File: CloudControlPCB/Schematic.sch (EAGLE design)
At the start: 4 parts, among them J1 AUDIO_JACK_TRRSSMD_RA, U1 LPC4088FBD208, U2 SGTL5000XNLA3R2

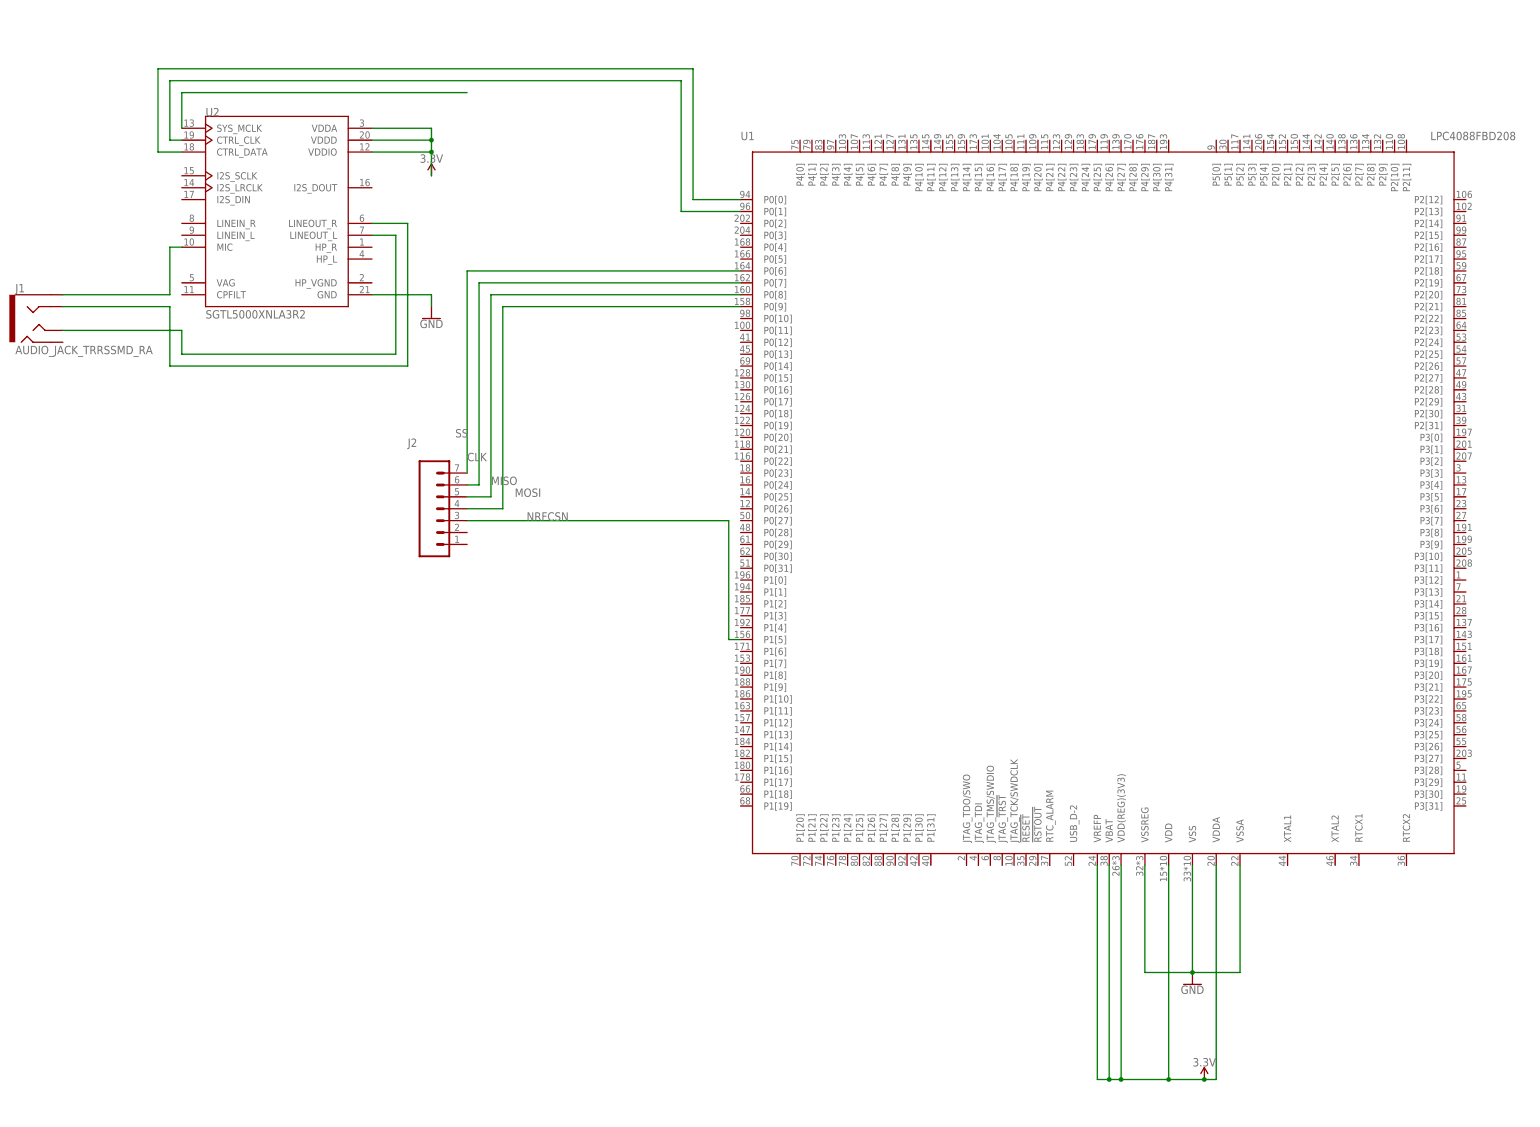
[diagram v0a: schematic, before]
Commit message: Added connections to DAC for I2S
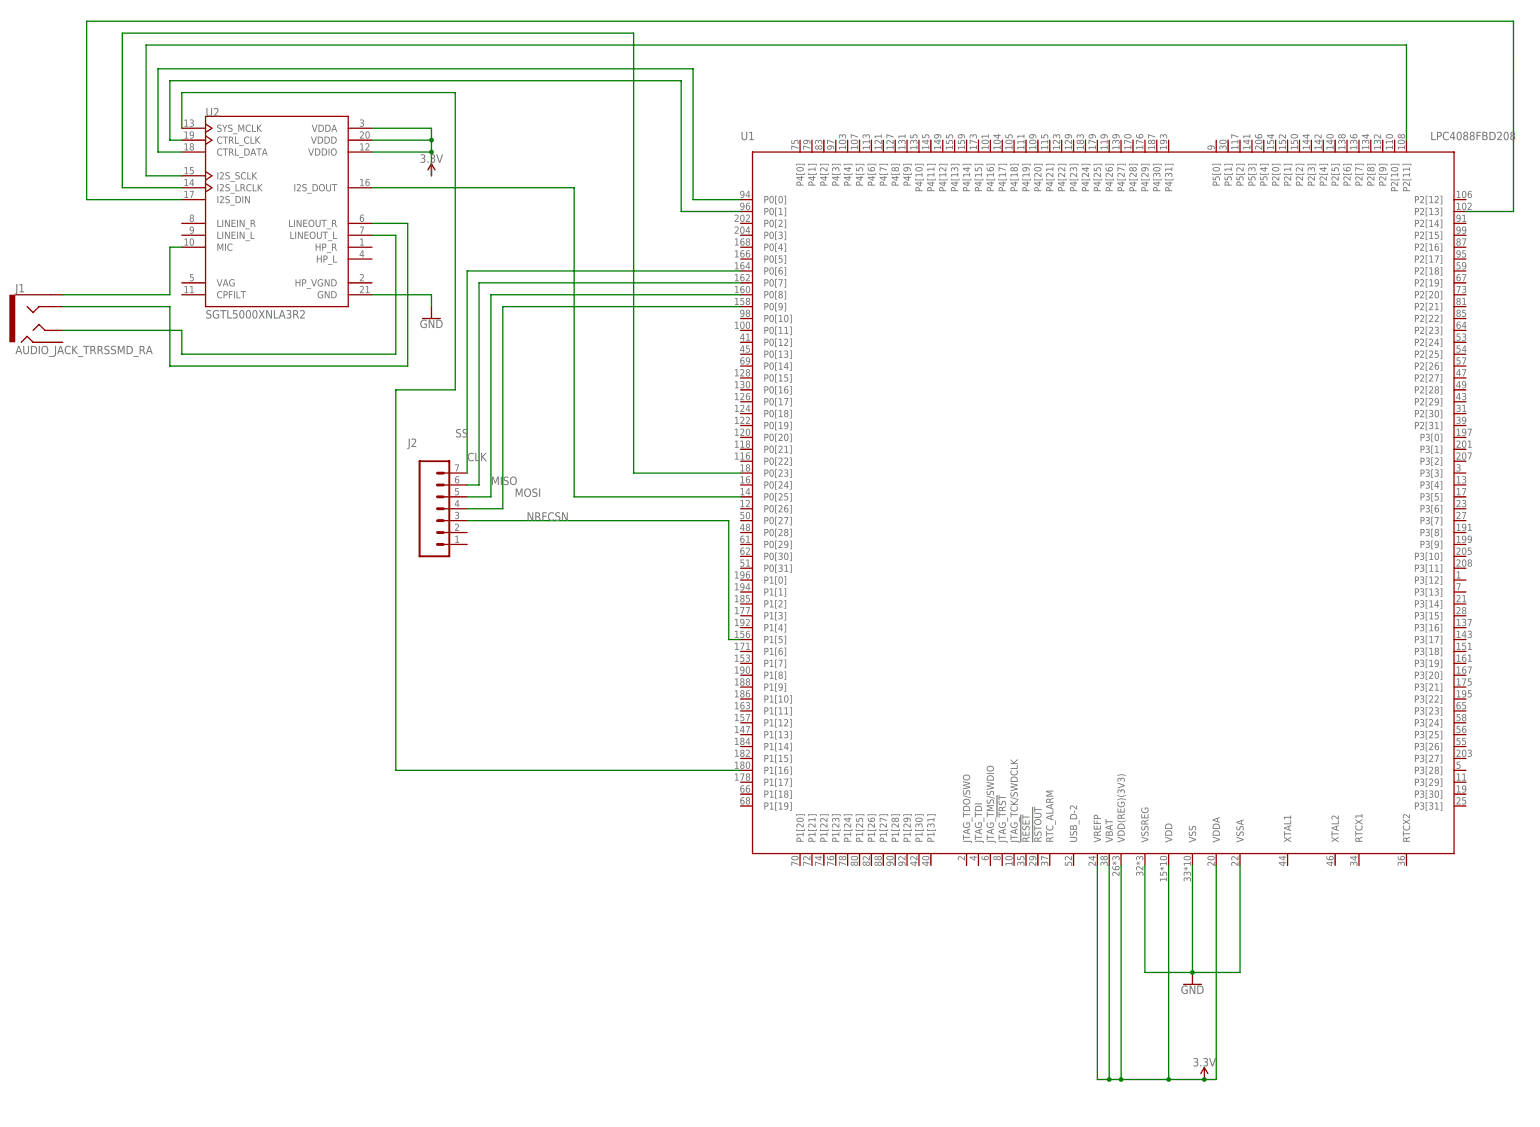
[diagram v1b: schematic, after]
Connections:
- new net N$10: U1.P2[11], U2.I2S_SCLK
- new net N$11: U1.P0[23], U2.I2S_LRCLK
- new net N$4: U1.P0[25], U2.I2S_DOUT
- new net N$8: U1.P1[16], U2.SYS_MCLK
- net N$5: now also U1.P2[13], U2.I2S_DIN; no longer U2.SYS_MCLK
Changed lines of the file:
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@@
 <?xml version="1.0" encoding="utf-8"?>
 <!DOCTYPE eagle SYSTEM "eagle.dtd">
-<eagle version="9.2.1">
+<eagle version="9.2.0">
 <drawing>
 <settings>
@@
 </plain>
 <instances>
-<instance part="U1" gate="G$1" x="73.66" y="35.56" smashed="yes">
+<instance part="U1" gate="G$1" x="73.66" y="35.56">
 <attribute name="NAME" x="-5.08" y="111.76" size="1.778" layer="95" font="vector"/>
 <attribute name="VALUE" x="142.24" y="111.76" size="1.778" layer="96" font="vector"/>
 </instance>
-<instance part="J2" gate="G$1" x="-68.58" y="30.48" smashed="yes">
+<instance part="J2" gate="G$1" x="-68.58" y="30.48">
 <attribute name="VALUE" x="-73.66" y="20.574" size="1.778" layer="96" font="vector"/>
 <attribute name="NAME" x="-76.2" y="46.228" size="1.778" layer="95" font="vector"/>
 </instance>
-<instance part="GND1" gate="1" x="91.44" y="-68.58" smashed="yes">
+<instance part="GND1" gate="1" x="91.44" y="-68.58">
 <attribute name="VALUE" x="91.44" y="-68.834" size="1.778" layer="96" align="top-center"/>
 </instance>
-<instance part="SUPPLY1" gate="G$1" x="93.98" y="-88.9" smashed="yes">
+<instance part="SUPPLY1" gate="G$1" x="93.98" y="-88.9">
 <attribute name="VALUE" x="93.98" y="-86.106" size="1.778" layer="96" align="bottom-center"/>
 </instance>
-<instance part="U2" gate="G$1" x="-104.14" y="96.52" smashed="yes">
+<instance part="U2" gate="G$1" x="-104.14" y="96.52">
 <attribute name="NAME" x="-119.3827" y="116.8435" size="1.778309375" layer="95"/>
 <attribute name="VALUE" x="-119.3806" y="73.6591" size="1.77806875" layer="96"/>
 </instance>
-<instance part="J1" gate="G$1" x="-154.94" y="73.66" smashed="yes">
+<instance part="J1" gate="G$1" x="-154.94" y="73.66">
 <attribute name="NAME" x="-160.02" y="79.248" size="1.778" layer="95" font="vector"/>
 <attribute name="VALUE" x="-160.02" y="66.04" size="1.778" layer="96" font="vector"/>
 </instance>
-<instance part="GND2" gate="1" x="-71.12" y="73.66" smashed="yes">
+<instance part="GND2" gate="1" x="-71.12" y="73.66">
 <attribute name="VALUE" x="-71.12" y="73.406" size="1.778" layer="96" align="top-center"/>
 </instance>
-<instance part="SUPPLY2" gate="G$1" x="-71.12" y="104.14" smashed="yes">
+<instance part="SUPPLY2" gate="G$1" x="-71.12" y="104.14">
 <attribute name="VALUE" x="-71.12" y="106.934" size="1.778" layer="96" align="bottom-center"/>
 </instance>
@@
 </segment>
 </net>
-<net name="N$5" class="0">
+<net name="N$8" class="0">
 <segment>
 <pinref part="U2" gate="G$1" pin="SYS_MCLK"/>
 <wire x1="-124.46" y1="114.3" x2="-124.46" y2="121.92" width="0.1524" layer="91"/>
-<wire x1="-124.46" y1="121.92" x2="-63.5" y2="121.92" width="0.1524" layer="91"/>
-</segment>
-</net>
+<pinref part="U1" gate="G$1" pin="P1[16]"/>
+<wire x1="-5.08" y1="-22.86" x2="-78.74" y2="-22.86" width="0.1524" layer="91"/>
+<wire x1="-78.74" y1="-22.86" x2="-78.74" y2="58.42" width="0.1524" layer="91"/>
+<wire x1="-78.74" y1="58.42" x2="-66.04" y2="58.42" width="0.1524" layer="91"/>
+<wire x1="-66.04" y1="58.42" x2="-66.04" y2="121.92" width="0.1524" layer="91"/>
+<wire x1="-124.46" y1="121.92" x2="-66.04" y2="121.92" width="0.1524" layer="91"/>
+</segment>
+</net>
+<net name="N$4" class="0">
+<segment>
+<pinref part="U1" gate="G$1" pin="P0[25]"/>
+<wire x1="-5.08" y1="35.56" x2="-40.64" y2="35.56" width="0.1524" layer="91"/>
+<wire x1="-40.64" y1="35.56" x2="-40.64" y2="101.6" width="0.1524" layer="91"/>
+<pinref part="U2" gate="G$1" pin="I2S_DOUT"/>
+<wire x1="-40.64" y1="101.6" x2="-83.82" y2="101.6" width="0.1524" layer="91"/>
+</segment>
+</net>
+<net name="N$5" class="0">
+<segment>
+<wire x1="-144.78" y1="137.16" x2="-144.78" y2="99.06" width="0.1524" layer="91"/>
+<pinref part="U2" gate="G$1" pin="I2S_DIN"/>
+<wire x1="-144.78" y1="99.06" x2="-124.46" y2="99.06" width="0.1524" layer="91"/>
+<pinref part="U1" gate="G$1" pin="P2[13]"/>
+<wire x1="149.86" y1="96.52" x2="160.02" y2="96.52" width="0.1524" layer="91"/>
+<wire x1="160.02" y1="96.52" x2="160.02" y2="127" width="0.1524" layer="91"/>
+<wire x1="160.02" y1="127" x2="160.02" y2="129.54" width="0.1524" layer="91"/>
+<wire x1="-144.78" y1="137.16" x2="160.02" y2="137.16" width="0.1524" layer="91"/>
+<wire x1="160.02" y1="137.16" x2="160.02" y2="129.54" width="0.1524" layer="91"/>
+</segment>
+</net>
+<net name="N$10" class="0">
+<segment>
+<pinref part="U2" gate="G$1" pin="I2S_SCLK"/>
+<wire x1="-124.46" y1="104.14" x2="-132.08" y2="104.14" width="0.1524" layer="91"/>
+<wire x1="-132.08" y1="104.14" x2="-132.08" y2="132.08" width="0.1524" layer="91"/>
+<pinref part="U1" gate="G$1" pin="P2[11]"/>
+<wire x1="-132.08" y1="132.08" x2="137.16" y2="132.08" width="0.1524" layer="91"/>
+<wire x1="137.16" y1="132.08" x2="137.16" y2="111.76" width="0.1524" layer="91"/>
+</segment>
+</net>
+<net name="N$11" class="0">
+<segment>
+<pinref part="U1" gate="G$1" pin="P0[23]"/>
+<wire x1="-5.08" y1="40.64" x2="-27.94" y2="40.64" width="0.1524" layer="91"/>
+<wire x1="-27.94" y1="40.64" x2="-27.94" y2="134.62" width="0.1524" layer="91"/>
+<wire x1="-27.94" y1="134.62" x2="-137.16" y2="134.62" width="0.1524" layer="91"/>
+<wire x1="-137.16" y1="134.62" x2="-137.16" y2="101.6" width="0.1524" layer="91"/>
+<pinref part="U2" gate="G$1" pin="I2S_LRCLK"/>
+<wire x1="-137.16" y1="101.6" x2="-124.46" y2="101.6" width="0.1524" layer="91"/>
+</segment>
+</net>

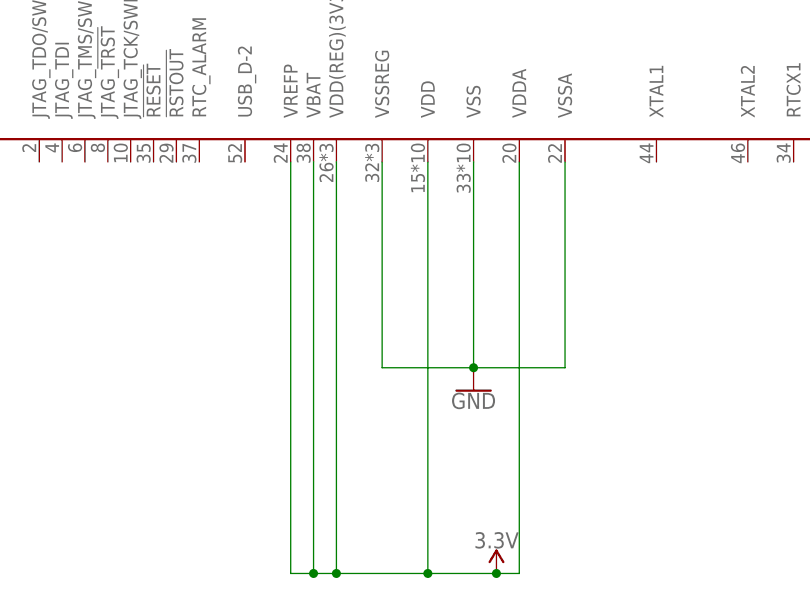
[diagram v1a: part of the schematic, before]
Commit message: Adjusted Vref and Vdda to have bypass capacitors
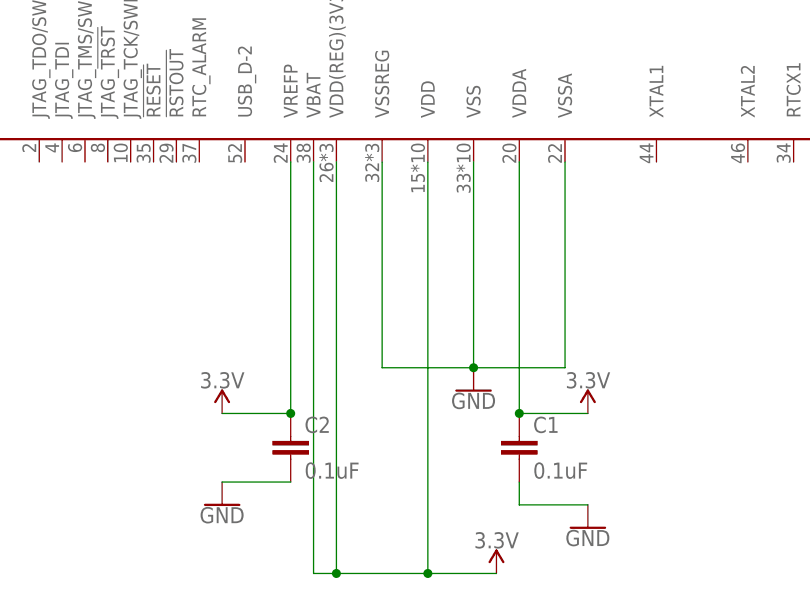
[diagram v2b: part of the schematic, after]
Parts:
- added C1, C2: 0.1uF, SparkFun-Capacitors:0.1UF-0603-25V-(+80/-20%)
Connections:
- net 3.3V: now also C1.1, C2.1
- net GND: now also C1.2, C2.2
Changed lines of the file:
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@@
 <part name="GND2" library="Homework1" deviceset="GND" device=""/>
 <part name="SUPPLY2" library="Homework1" deviceset="3.3V" device=""/>
+<part name="C1" library="SparkFun-Capacitors" deviceset="0.1UF" device="-0603-25V-(+80/-20%)" value="0.1uF"/>
+<part name="GND3" library="Homework1" deviceset="GND" device=""/>
+<part name="SUPPLY3" library="Homework1" deviceset="3.3V" device=""/>
+<part name="C2" library="SparkFun-Capacitors" deviceset="0.1UF" device="-0603-25V-(+80/-20%)" value="0.1uF"/>
+<part name="GND4" library="Homework1" deviceset="GND" device=""/>
+<part name="SUPPLY4" library="Homework1" deviceset="3.3V" device=""/>
 </parts>
 <sheets>
@@
 <instance part="SUPPLY2" gate="G$1" x="-71.12" y="104.14">
 <attribute name="VALUE" x="-71.12" y="106.934" size="1.778" layer="96" align="bottom-center"/>
+</instance>
+<instance part="C1" gate="G$1" x="96.52" y="-76.2">
+<attribute name="NAME" x="98.044" y="-73.279" size="1.778" layer="95" font="vector"/>
+<attribute name="VALUE" x="98.044" y="-78.359" size="1.778" layer="96" font="vector"/>
+</instance>
+<instance part="GND3" gate="1" x="104.14" y="-83.82">
+<attribute name="VALUE" x="104.14" y="-84.074" size="1.778" layer="96" align="top-center"/>
+</instance>
+<instance part="SUPPLY3" gate="G$1" x="104.14" y="-71.12">
+<attribute name="VALUE" x="104.14" y="-68.326" size="1.778" layer="96" align="bottom-center"/>
+</instance>
+<instance part="C2" gate="G$1" x="71.12" y="-76.2">
+<attribute name="NAME" x="72.644" y="-73.279" size="1.778" layer="95" font="vector"/>
+<attribute name="VALUE" x="72.644" y="-78.359" size="1.778" layer="96" font="vector"/>
+</instance>
+<instance part="GND4" gate="1" x="63.5" y="-81.28">
+<attribute name="VALUE" x="63.5" y="-81.534" size="1.778" layer="96" align="top-center"/>
+</instance>
+<instance part="SUPPLY4" gate="G$1" x="63.5" y="-71.12">
+<attribute name="VALUE" x="63.5" y="-68.326" size="1.778" layer="96" align="bottom-center"/>
 </instance>
 </instances>
@@
 <wire x1="-71.12" y1="78.74" x2="-71.12" y2="76.2" width="0.1524" layer="91"/>
 </segment>
+<segment>
+<pinref part="C1" gate="G$1" pin="2"/>
+<wire x1="96.52" y1="-78.74" x2="96.52" y2="-81.28" width="0.1524" layer="91"/>
+<wire x1="96.52" y1="-81.28" x2="104.14" y2="-81.28" width="0.1524" layer="91"/>
+<pinref part="GND3" gate="1" pin="GND"/>
+</segment>
+<segment>
+<pinref part="C2" gate="G$1" pin="2"/>
+<wire x1="71.12" y1="-78.74" x2="63.5" y2="-78.74" width="0.1524" layer="91"/>
+<pinref part="GND4" gate="1" pin="GND"/>
+</segment>
 </net>
 <net name="3.3V" class="0">
@@
 <wire x1="86.36" y1="-43.18" x2="86.36" y2="-88.9" width="0.1524" layer="91"/>
 <wire x1="86.36" y1="-88.9" x2="93.98" y2="-88.9" width="0.1524" layer="91"/>
-<pinref part="U1" gate="G$1" pin="VDDA"/>
-<wire x1="96.52" y1="-43.18" x2="96.52" y2="-88.9" width="0.1524" layer="91"/>
-<wire x1="96.52" y1="-88.9" x2="93.98" y2="-88.9" width="0.1524" layer="91"/>
-<junction x="93.98" y="-88.9"/>
-<pinref part="U1" gate="G$1" pin="VREFP"/>
-<wire x1="71.12" y1="-43.18" x2="71.12" y2="-88.9" width="0.1524" layer="91"/>
-<wire x1="71.12" y1="-88.9" x2="73.66" y2="-88.9" width="0.1524" layer="91"/>
 <junction x="86.36" y="-88.9"/>
 <pinref part="U1" gate="G$1" pin="VDD(REG)(3V3)"/>
@@
 <pinref part="U1" gate="G$1" pin="VBAT"/>
 <wire x1="73.66" y1="-43.18" x2="73.66" y2="-88.9" width="0.1524" layer="91"/>
-<junction x="73.66" y="-88.9"/>
 </segment>
 <segment>
@@
 <junction x="-71.12" y="109.22"/>
 </segment>
-</net>
+<segment>
+<pinref part="U1" gate="G$1" pin="VDDA"/>
+<pinref part="C1" gate="G$1" pin="1"/>
+<wire x1="96.52" y1="-43.18" x2="96.52" y2="-71.12" width="0.1524" layer="91"/>
+<wire x1="96.52" y1="-71.12" x2="104.14" y2="-71.12" width="0.1524" layer="91"/>
+<junction x="96.52" y="-71.12"/>
+<pinref part="SUPPLY3" gate="G$1" pin="3.3V"/>
+</segment>
+<segment>
+<pinref part="U1" gate="G$1" pin="VREFP"/>
+<pinref part="C2" gate="G$1" pin="1"/>
+<wire x1="71.12" y1="-43.18" x2="71.12" y2="-71.12" width="0.1524" layer="91"/>
+<wire x1="71.12" y1="-71.12" x2="63.5" y2="-71.12" width="0.1524" layer="91"/>
+<junction x="71.12" y="-71.12"/>
+<pinref part="SUPPLY4" gate="G$1" pin="3.3V"/>
+</segment>
+</net>
